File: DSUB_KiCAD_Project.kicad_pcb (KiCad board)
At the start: 4 copper layers, 112.2 x 87.2 mm, 6 parts, among them J1 DB37_Female, J2 DB37_Female, J3 DB37_Female, J4 DB37_Female, J5 DB37_Female, J6 DB37_Female

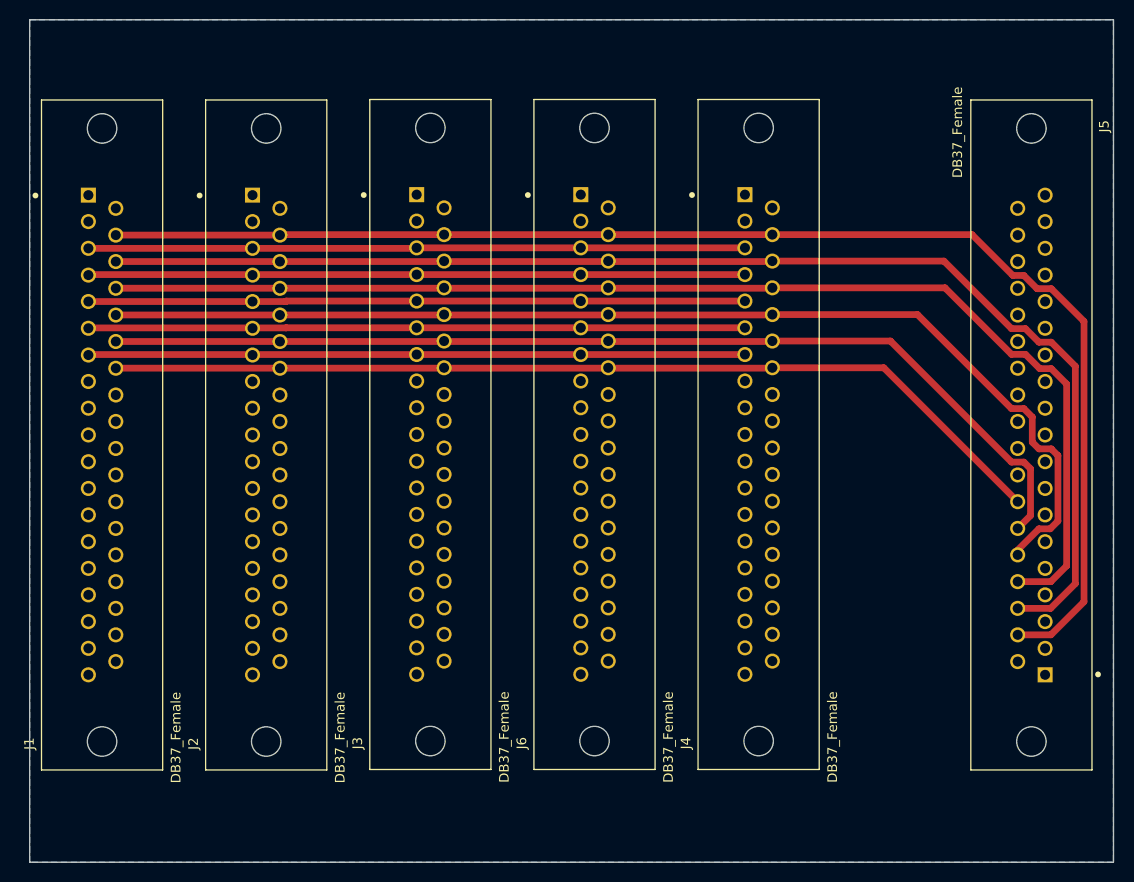
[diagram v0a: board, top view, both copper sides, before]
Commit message: Changed layout
Layout was changed. Now we have planes for ground, 5v, and 3v3. hopefully current wont be an issue
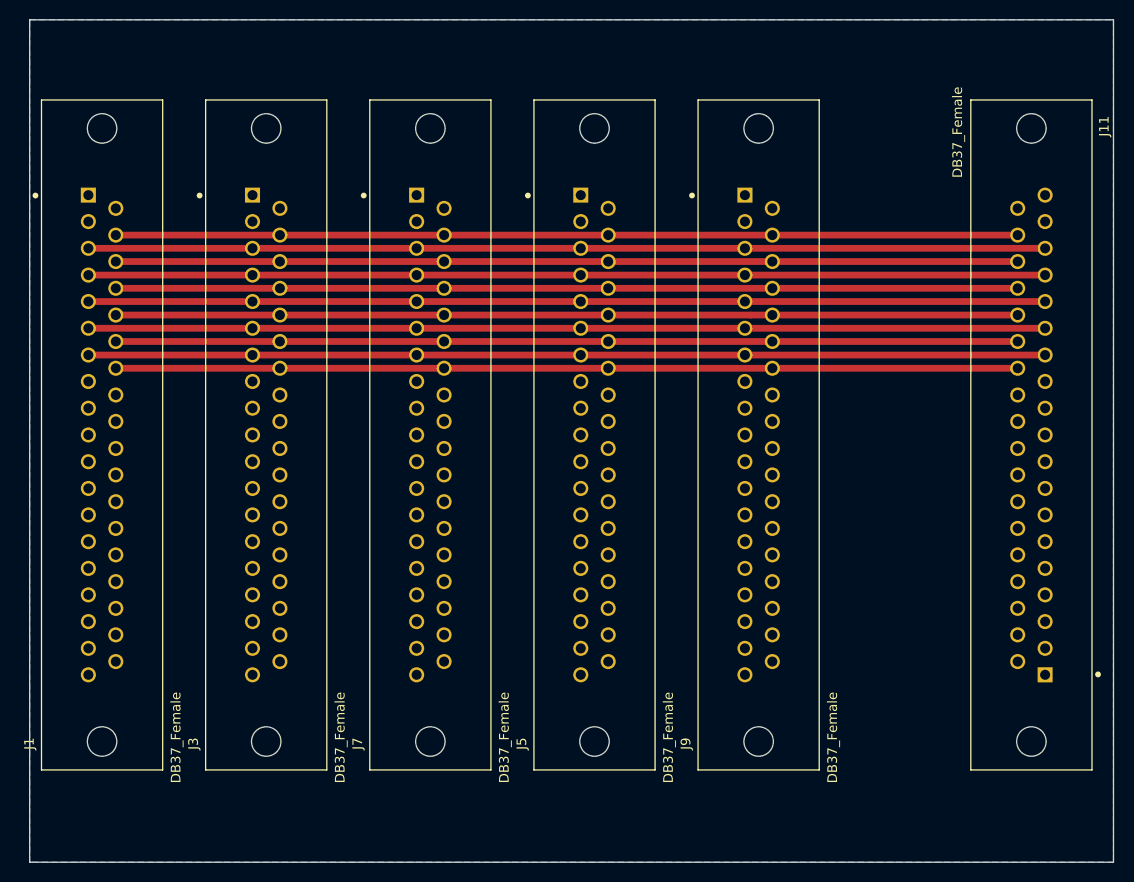
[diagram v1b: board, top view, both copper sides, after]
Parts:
- removed J2, J4, J6: DB37_Female, 1-747301-6:TE_1-747301-6
- added J11: DB37_Female, 1-747301-6:TE_1-747301-6, F.Cu at (196.2, 83.2)
- added J7: DB37_Female, 1-747301-6:TE_1-747301-6, F.Cu at (134.0, 83.2)
- added J9: DB37_Female, 1-747301-6:TE_1-747301-6, F.Cu at (168.0, 83.2)
- moved J5 45.2 mm to (151.0, 83.2), turned to 90 degrees
- moved J3 17.0 mm to (117.0, 83.2)
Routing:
- net +3V3: track 243.5 -> 0.00 mm
- net +5V: track 242.0 -> 0.00 mm
- net /tmosi: track 141.3 -> 93.4 mm
- net /tmiso: track 143.9 -> 99.1 mm
- net /t_clk: track 133.5 -> 93.4 mm
- net /SWCLK: track 127.2 -> 93.4 mm
- net /SWDIo: track 127.9 -> 99.1 mm
- net /Alert_sda: track 117.9 -> 93.4 mm
- net /Alert_scl: track 120.1 -> 99.1 mm
- net /Alert_active: track 113.8 -> 99.1 mm
- net /NRT: track 107.0 -> 93.4 mm
- net /Fire: track 106.6 -> 99.1 mm
- net /Fire_Redundant: track 99.2 -> 93.4 mm
- added copper zone on B.Cu, net +3V3
- added copper zone on 5v, net +5V
- added copper zone on Ground, net GND
- removed copper zone on B.Cu, net GND
